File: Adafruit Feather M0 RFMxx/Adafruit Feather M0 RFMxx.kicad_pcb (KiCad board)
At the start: 2 copper layers, 50.8 x 22.9 mm, 44 parts, among them SW1 SPST_TACT-KMR2, U2 AP2112K-3.3, U3 MCP73831T-2ACI/OT, U4 RFM69HCW, X1 JSTPH, X2 32.768, X3 microUSB, X4 uFL

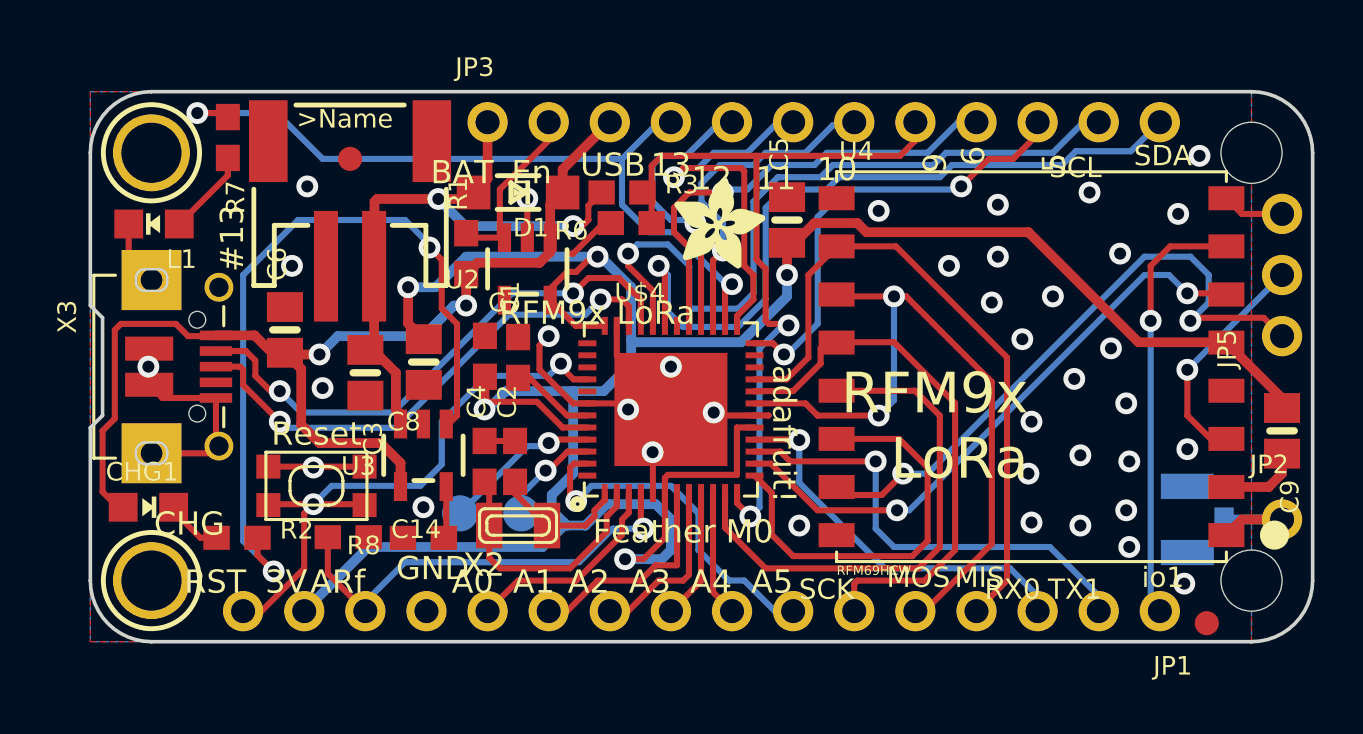
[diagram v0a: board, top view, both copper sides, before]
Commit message: Started adding qwiic connector.
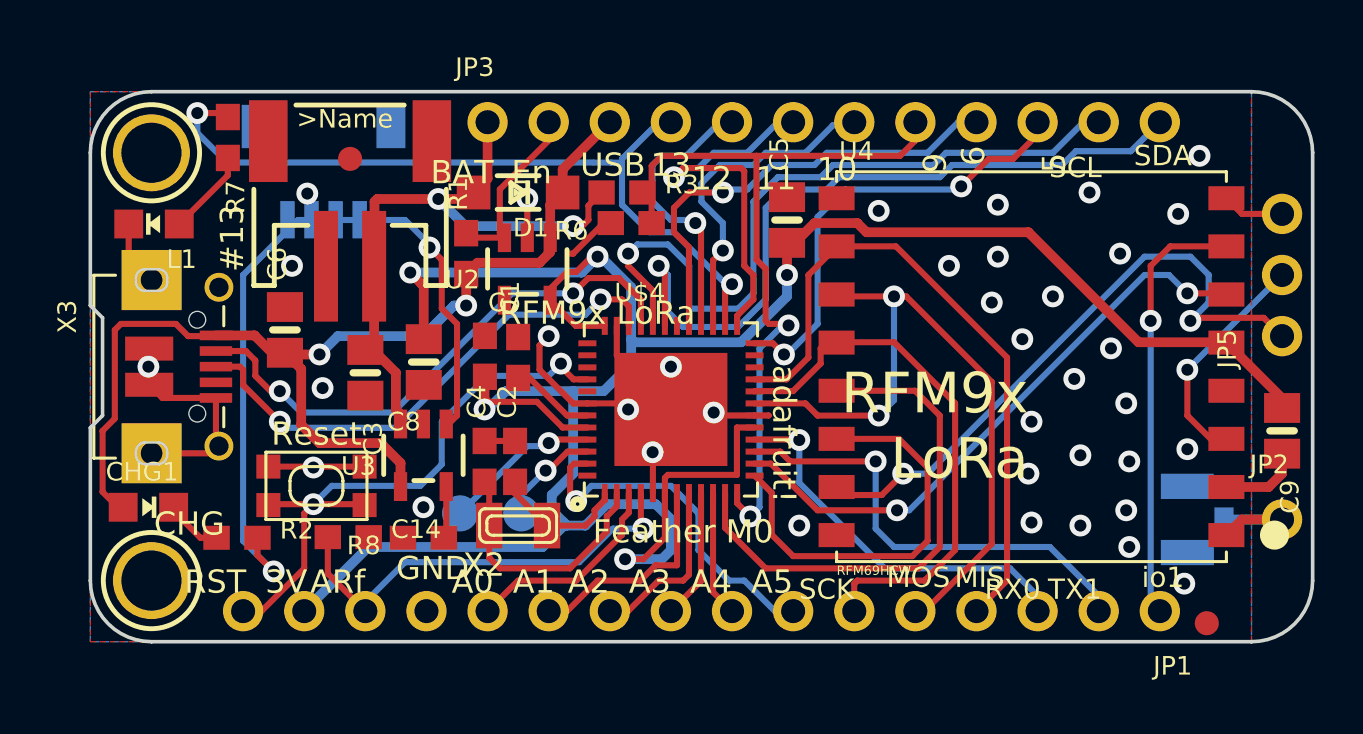
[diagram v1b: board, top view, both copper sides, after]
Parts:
- removed @HOLE0, @HOLE1: , 
- removed U$12, U$7: , Adafruit Feather M0 RFMxx:ADAFRUIT_3.5MM
- removed U$13: , Adafruit Feather M0 RFMxx:PCBFEAT-REV-040
- removed U$9: , Adafruit Feather M0 RFMxx:FEATHERLOGO
- added JP7: SM04B-SRSS-TB(LF)(SN), SM04B-SRSS-TB(LFSN), B.Cu at (129.8, 94.2)
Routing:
- net /D13: track 32.1 -> 32.7 mm

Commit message: Qwiic connector addition completed
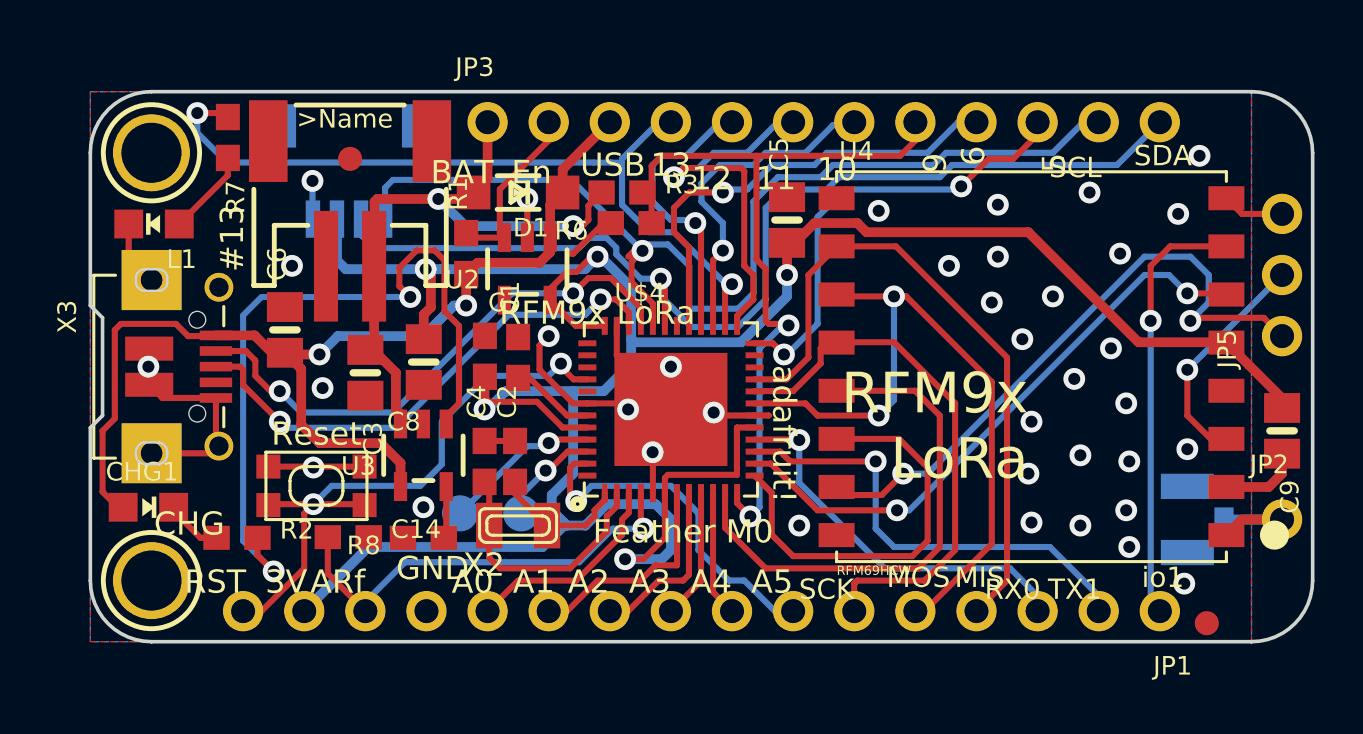
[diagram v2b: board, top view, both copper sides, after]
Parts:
- moved JP7 1.06 mm to (130.9, 94.2)
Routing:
- net /SCL: track 30.9 -> 44.4 mm
- net /SDA: track 31.1 -> 44.2 mm
- net +3V3: track 107.9 -> 112.9 mm
- net GND: track 45.0 -> 46.6 mm
- net Net-(R2-Pad2): track 31.8 -> 31.0 mm

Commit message: Took a look at fitting in via's needed to breakout pins 22 & 23. Looks like it can be done without a lot of work. Likely will need to shrink a couple of existing via's.
DRC complained about some things that haven't changed from the original Adafruit
design (USB connector mounting holes too close to something, and maybe something
else.
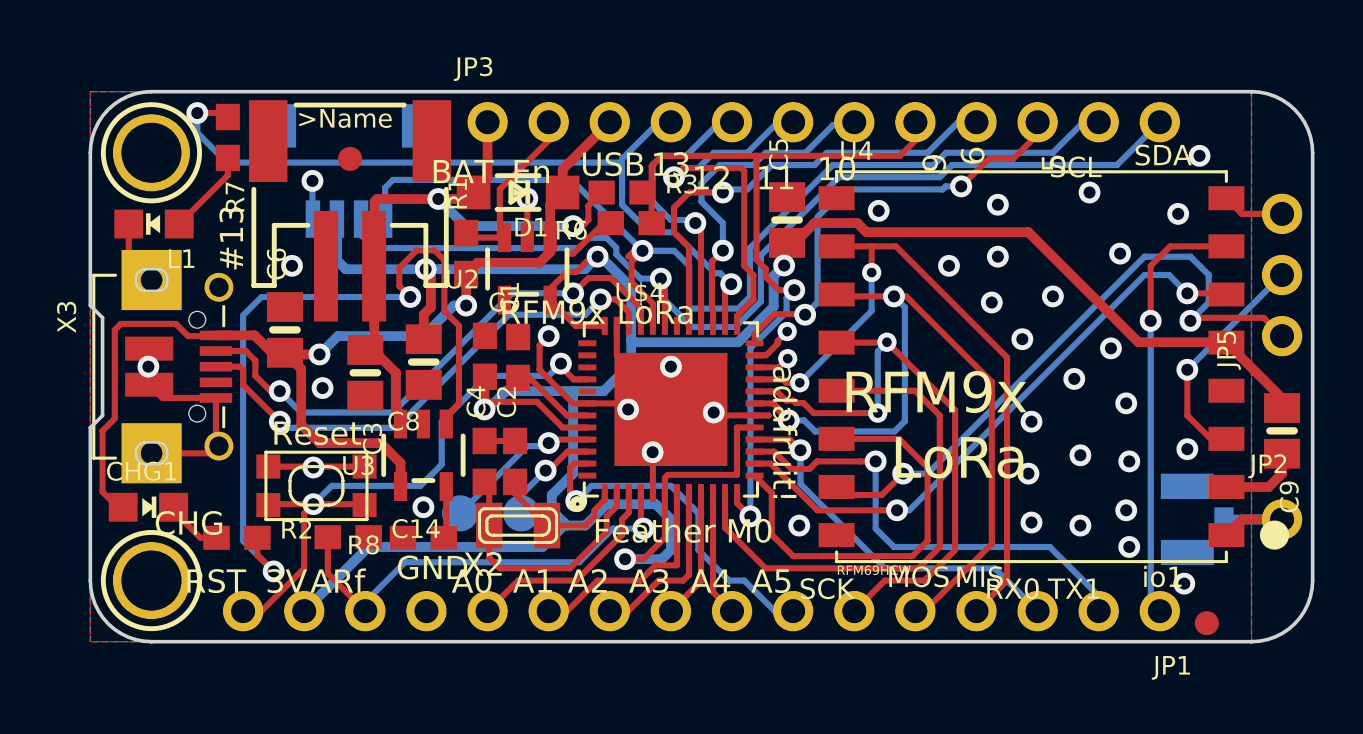
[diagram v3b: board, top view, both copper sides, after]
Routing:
- net /SCK: track 22.6 -> 25.8 mm, vias 0 -> 2
- net /D2: track 0.00 -> 1.83 mm, vias 0 -> 1
- net /MOSI: track 29.7 -> 31.4 mm
- net Net-(U$4-Pad22): track 0.00 -> 1.53 mm, vias 0 -> 1
- net /MISO: track 27.8 -> 29.2 mm, vias 0 -> 2
- net /SCL: track 44.4 -> 43.1 mm
- net /SDA: track 44.2 -> 43.1 mm
- net /D0: track 16.2 -> 15.5 mm
- net /D5: track 18.9 -> 18.3 mm
